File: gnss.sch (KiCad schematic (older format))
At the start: 12 parts, among them U2301 MAX-M8Q

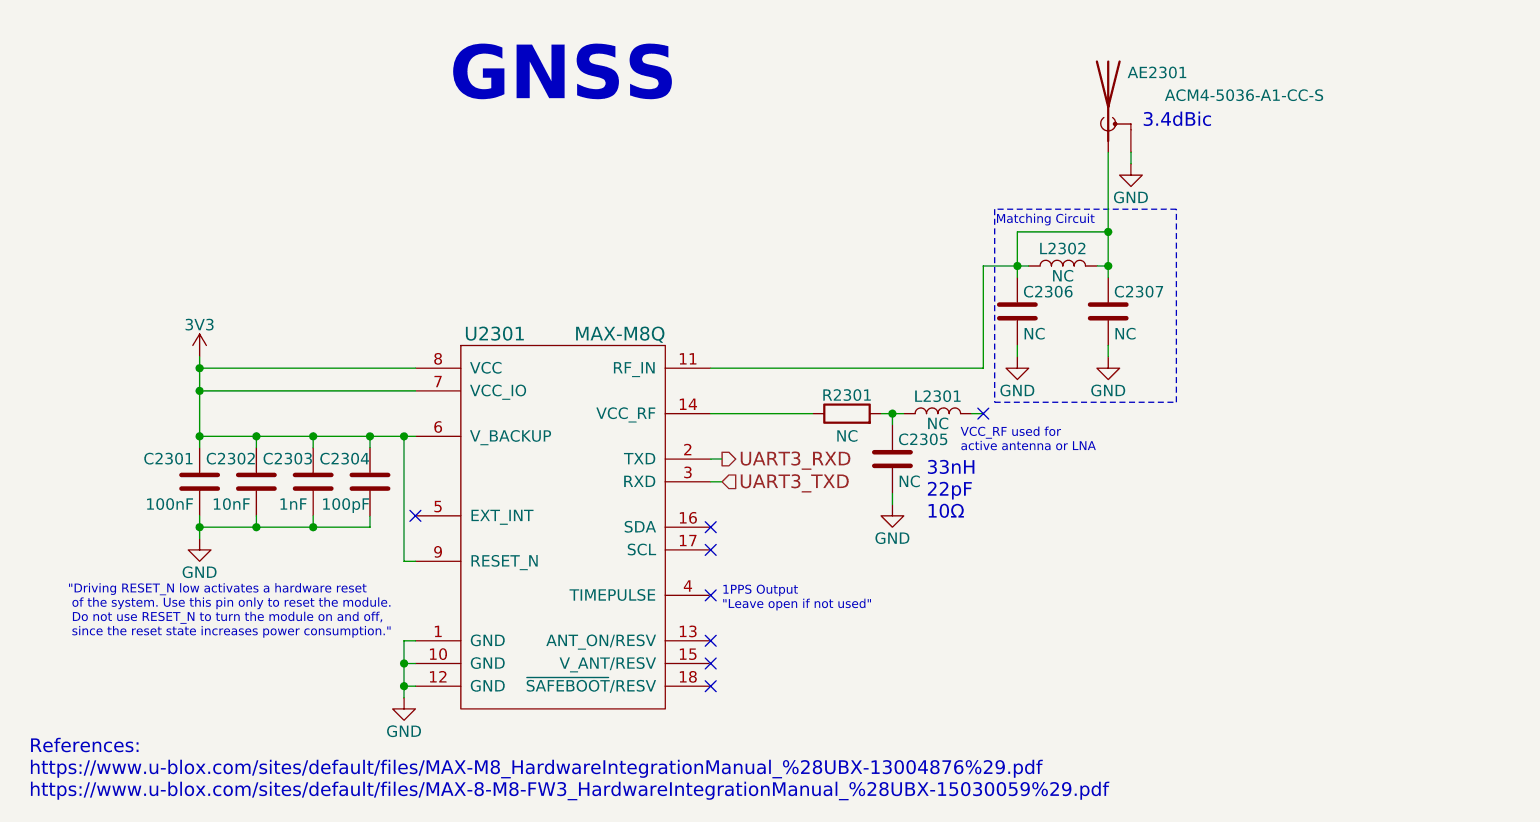
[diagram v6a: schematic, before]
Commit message: Add AC coupling caps to the HDMI_AUXP/N diff pair which were mistakenly left out, fix a couple typos/errors that were made when transitioning to the new top-leve sheet, make the M.2s' I2C RX TX hierarchical signals consistent and clearer
Hopefully all lingering errors have been caught, this will likely be the schematic commit that gets reviewed (fingers crossed).
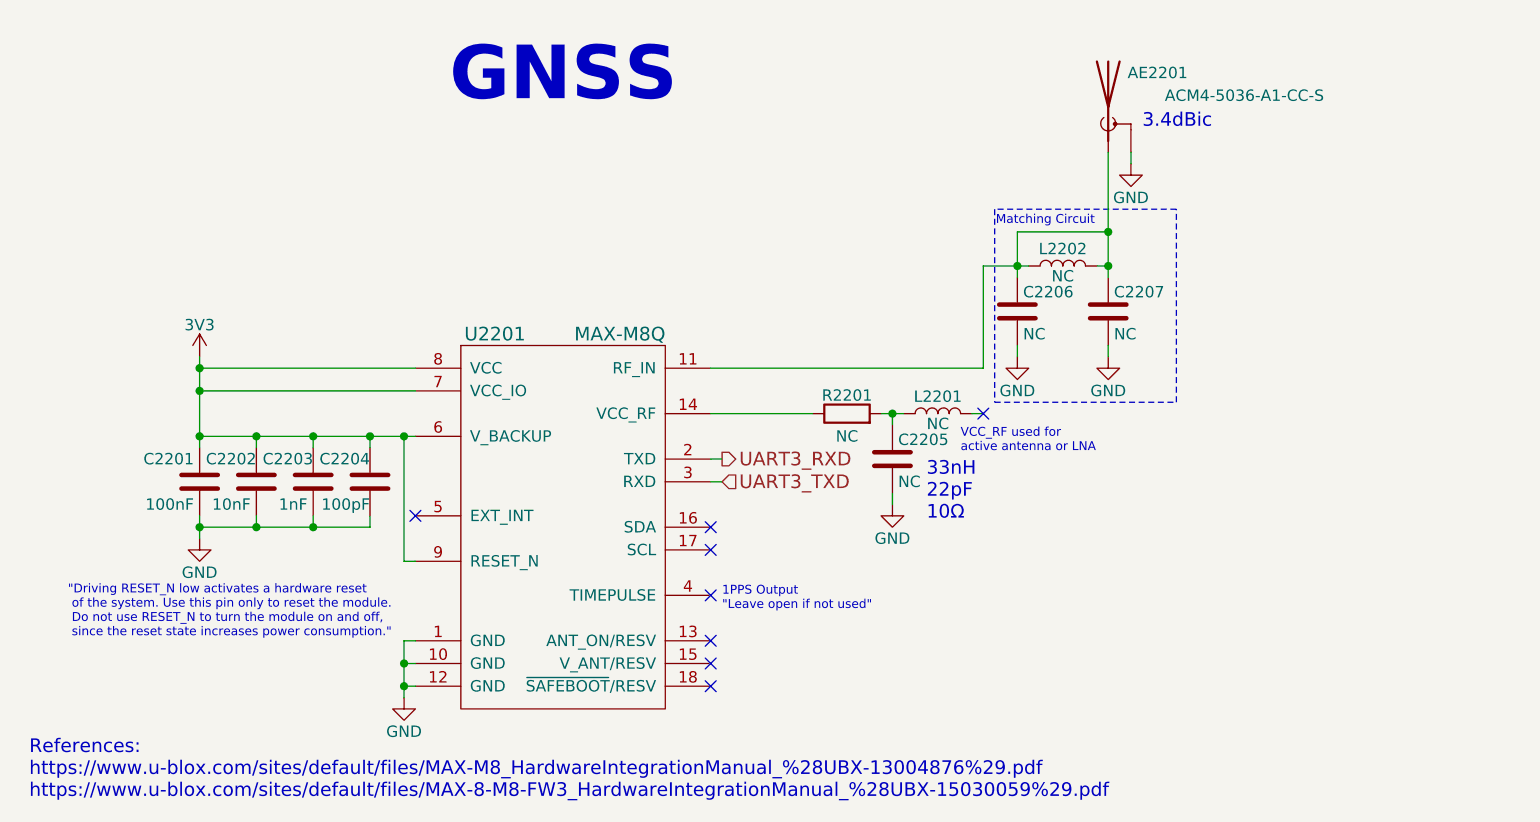
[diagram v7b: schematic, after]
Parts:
- renumbered AE2301 to AE2201, C2301 to C2201, C2302 to C2202, C2303 to C2203, C2304 to C2204, C2305 to C2205, C2306 to C2206, C2307 to C2207, L2301 to L2201, L2302 to L2202, R2301 to R2201, U2301 to U2201
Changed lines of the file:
@@
 $Descr A4 11693 8268
 encoding utf-8
-Sheet 23 24
+Sheet 22 24
 Title "GNSS"
 Date "2018-06-14"
@@
 $EndDescr
 $Comp
-L GND #PWR2303
+L GND #PWR0342
 U 1 1 5B0E0D78
 P 4800 4700
-F 0 "#PWR2303" H 4800 4450 50  0001 C CNN
+F 0 "#PWR0342" H 4800 4450 50  0001 C CNN
 F 1 "GND" H 4800 4550 50  0000 C CNN
 F 2 "" H 4800 4700 50  0001 C CNN
@@
 3.4dBic
 $Comp
-L 3V3 #PWR2301
+L 3V3 #PWR0343
 U 1 1 5B0E6D0E
 P 3900 3200
-F 0 "#PWR2301" H 3900 3050 50  0001 C CNN
+F 0 "#PWR0343" H 3900 3050 50  0001 C CNN
 F 1 "3V3" H 3900 3340 50  0000 C CNN
 F 2 "" H 3900 3200 50  0001 C CNN
@@
 NoConn ~ 6150 4450
 $Comp
-L C C2301
+L C C2201
 U 1 1 5B0ED9E5
 P 3900 3750
-F 0 "C2301" H 3925 3850 50  0000 L CNN
+F 0 "C2201" H 3925 3850 50  0000 L CNN
 F 1 "100nF" H 3925 3650 50  0000 L CNN
 F 2 "Capacitors_SMD:C_0603" H 3938 3600 50  0001 C CNN
@@
 $EndComp
 $Comp
-L GND #PWR2302
+L GND #PWR0344
 U 1 1 5B0EDAF7
 P 3900 4000
-F 0 "#PWR2302" H 3900 3750 50  0001 C CNN
+F 0 "#PWR0344" H 3900 3750 50  0001 C CNN
 F 1 "GND" H 3900 3850 50  0000 C CNN
 F 2 "" H 3900 4000 50  0001 C CNN
@@
 Connection ~ 4800 3550
 $Comp
-L C C2302
+L C C2202
 U 1 1 5B1028D6
 P 4150 3750
-F 0 "C2302" H 4150 3850 50  0000 L CNN
+F 0 "C2202" H 4150 3850 50  0000 L CNN
 F 1 "10nF" H 4175 3650 50  0000 L CNN
 F 2 "Capacitors_SMD:C_0603" H 4188 3600 50  0001 C CNN
@@
 $EndComp
 $Comp
-L C C2303
+L C C2203
 U 1 1 5B102929
 P 4400 3750
-F 0 "C2303" H 4400 3850 50  0000 L CNN
+F 0 "C2203" H 4400 3850 50  0000 L CNN
 F 1 "1nF" H 4425 3650 50  0000 L CNN
 F 2 "Capacitors_SMD:C_0603" H 4438 3600 50  0001 C CNN
@@
 $EndComp
 $Comp
-L C C2304
+L C C2204
 U 1 1 5B1029AE
 P 4650 3750
-F 0 "C2304" H 4650 3850 50  0000 L CNN
+F 0 "C2204" H 4650 3850 50  0000 L CNN
 F 1 "100pF" H 4650 3650 50  0000 L CNN
 F 2 "Capacitors_SMD:C_0603" H 4688 3600 50  0001 C CNN
@@
 UART3_TXD
 $Comp
-L Antenna_Chip AE2301
+L Antenna_Chip AE2201
 U 1 1 5B123EED
 P 7900 2100
-F 0 "AE2301" H 8250 2250 50  0000 R CNN
+F 0 "AE2201" H 8250 2250 50  0000 R CNN
 F 1 "ACM4-5036-A1-CC-S" H 8850 2150 50  0000 R CNN
 F 2 "dvk-mx8m-bsb:ACM4-5036-A1-CC-S" H 7900 2200 50  0001 C CNN
@@
 $EndComp
 $Comp
-L GND #PWR2307
+L GND #PWR0345
 U 1 1 5B12431F
 P 8000 2350
-F 0 "#PWR2307" H 8000 2100 50  0001 C CNN
+F 0 "#PWR0345" H 8000 2100 50  0001 C CNN
 F 1 "GND" H 8000 2200 50  0000 C CNN
 F 2 "" H 8000 2350 50  0001 C CNN
@@
 	7350 3450 7300 3450
 $Comp
-L L L2301
+L L L2201
 U 1 1 5B103CD2
 P 7150 3450
-F 0 "L2301" V 7225 3450 50  0000 C CNN
+F 0 "L2201" V 7225 3450 50  0000 C CNN
 F 1 "NC" V 7105 3450 50  0000 C CNN
 F 2 "Inductors_SMD:L_0603" H 7150 3450 50  0001 C CNN
@@
 	6950 3850 6950 3800
 $Comp
-L GND #PWR2304
+L GND #PWR0346
 U 1 1 5B103EA0
 P 6950 3850
-F 0 "#PWR2304" H 6950 3600 50  0001 C CNN
+F 0 "#PWR0346" H 6950 3600 50  0001 C CNN
 F 1 "GND" H 6950 3700 50  0000 C CNN
 F 2 "" H 6950 3850 50  0001 C CNN
@@
 	6900 3450 7000 3450
 $Comp
-L C C2305
+L C C2205
 U 1 1 5B103D07
 P 6950 3650
-F 0 "C2305" H 6975 3735 50  0000 L CNN
+F 0 "C2205" H 6975 3735 50  0000 L CNN
 F 1 "NC" H 6975 3550 50  0000 L CNN
 F 2 "Capacitors_SMD:C_0603" H 6988 3500 50  0001 C CNN
@@
 $EndComp
 $Comp
-L R R2301
+L R R2201
 U 1 1 5B103CA5
 P 6750 3450
-F 0 "R2301" V 6830 3450 50  0000 C CNN
+F 0 "R2201" V 6830 3450 50  0000 C CNN
 F 1 "NC" V 6650 3450 50  0000 C CNN
 F 2 "Resistors_SMD:R_0603" V 6680 3450 50  0001 C CNN
@@
 33nH\n22pF\n10Ω
 $Comp
-L L L2302
+L L L2202
 U 1 1 5B2088FC
 P 7700 2800
-F 0 "L2302" V 7775 2800 50  0000 C CNN
+F 0 "L2202" V 7775 2800 50  0000 C CNN
 F 1 "NC" V 7655 2800 50  0000 C CNN
 F 2 "Inductors_SMD:L_0603" H 7700 2800 50  0001 C CNN
@@
 	7500 3200 7500 3150
 $Comp
-L GND #PWR2305
+L GND #PWR0347
 U 1 1 5B208BC0
 P 7500 3200
-F 0 "#PWR2305" H 7500 2950 50  0001 C CNN
+F 0 "#PWR0347" H 7500 2950 50  0001 C CNN
 F 1 "GND" H 7500 3050 50  0000 C CNN
 F 2 "" H 7500 3200 50  0001 C CNN
@@
 $EndComp
 $Comp
-L C C2306
+L C C2206
 U 1 1 5B208BC6
 P 7500 3000
-F 0 "C2306" H 7525 3085 50  0000 L CNN
+F 0 "C2206" H 7525 3085 50  0000 L CNN
 F 1 "NC" H 7525 2900 50  0000 L CNN
 F 2 "Capacitors_SMD:C_0603" H 7538 2850 50  0001 C CNN
@@
 	7900 3200 7900 3150
 $Comp
-L GND #PWR2306
+L GND #PWR0348
 U 1 1 5B208DA1
 P 7900 3200
-F 0 "#PWR2306" H 7900 2950 50  0001 C CNN
+F 0 "#PWR0348" H 7900 2950 50  0001 C CNN
 F 1 "GND" H 7900 3050 50  0000 C CNN
 F 2 "" H 7900 3200 50  0001 C CNN
@@
 $EndComp
 $Comp
-L C C2307
+L C C2207
 U 1 1 5B208DA7
 P 7900 3000
-F 0 "C2307" H 7925 3085 50  0000 L CNN
+F 0 "C2207" H 7925 3085 50  0000 L CNN
 F 1 "NC" H 7925 2900 50  0000 L CNN
 F 2 "Capacitors_SMD:C_0603" H 7938 2850 50  0001 C CNN
@@
 GNSS
 $Comp
-L MAX-M8 U2301
+L MAX-M8 U2201
 U 1 1 5B0DFDBF
 P 5500 3950
-F 0 "U2301" H 5200 4800 60  0000 C CNN
+F 0 "U2201" H 5200 4800 60  0000 C CNN
 F 1 "MAX-M8Q" H 5750 4800 60  0000 C CNN
 F 2 "dvk-mx8m-bsb:MAX-M8" H 6350 4300 60  0001 C CNN

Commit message: Move the WLAN+BT M.2 sheet back to page 18 rather than the last page (24)
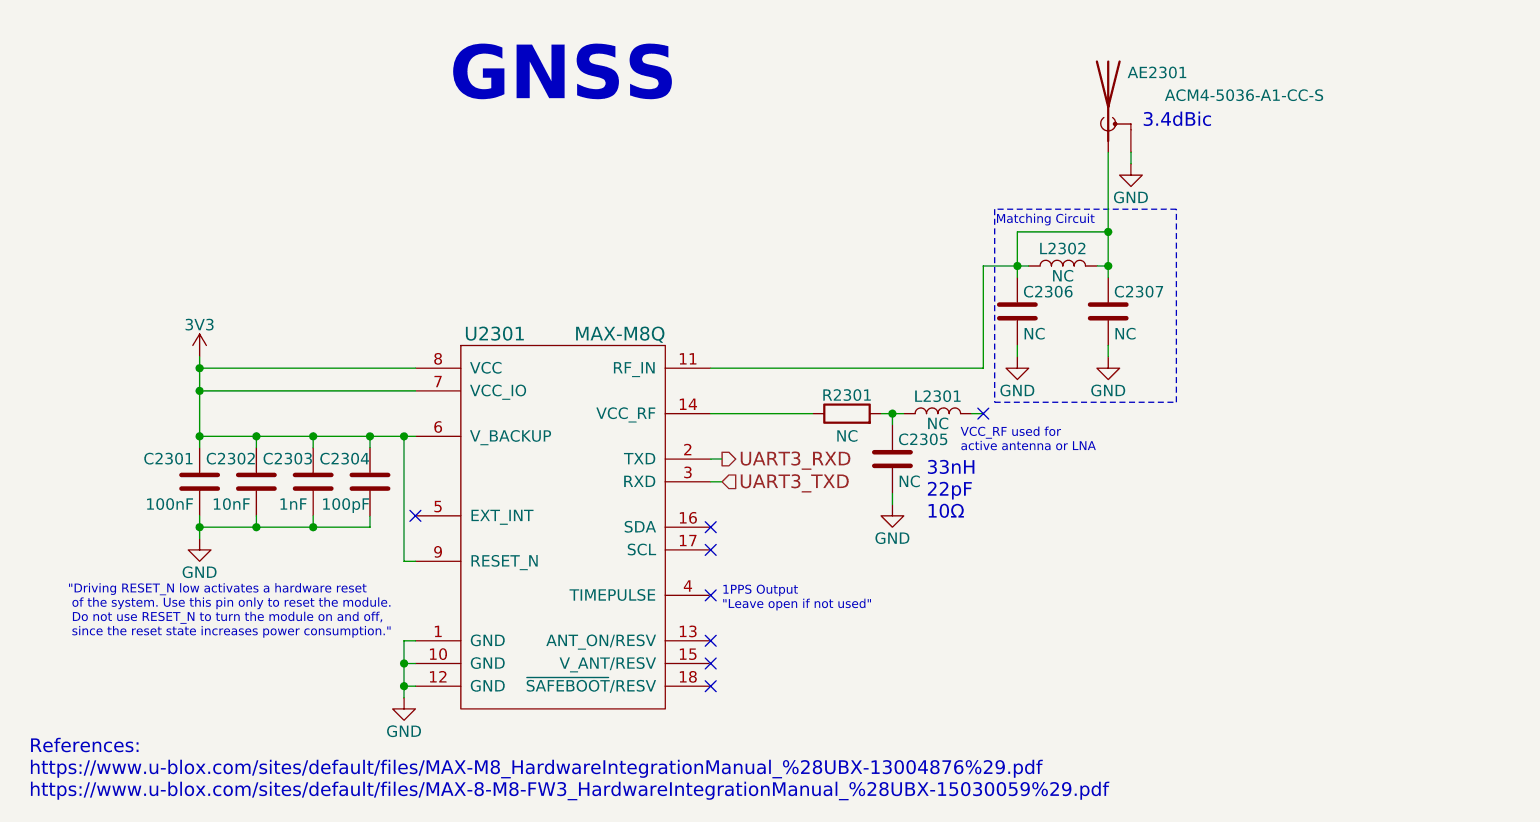
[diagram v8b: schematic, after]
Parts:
- renumbered AE2201 to AE2301, C2201 to C2301, C2202 to C2302, C2203 to C2303, C2204 to C2304, C2205 to C2305, C2206 to C2306, C2207 to C2307, L2201 to L2301, L2202 to L2302, R2201 to R2301, U2201 to U2301
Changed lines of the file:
@@
 $Descr A4 11693 8268
 encoding utf-8
-Sheet 22 24
+Sheet 23 24
 Title "GNSS"
-Date "2018-06-14"
+Date "2018-06-15"
 Rev "v0.1.0"
 Comp "Copyright 2018 GNU GPLv3"
@@
 $EndDescr
 $Comp
-L GND #PWR0342
+L GND #PWR0368
 U 1 1 5B0E0D78
 P 4800 4700
-F 0 "#PWR0342" H 4800 4450 50  0001 C CNN
+F 0 "#PWR0368" H 4800 4450 50  0001 C CNN
 F 1 "GND" H 4800 4550 50  0000 C CNN
 F 2 "" H 4800 4700 50  0001 C CNN
@@
 3.4dBic
 $Comp
-L 3V3 #PWR0343
+L 3V3 #PWR0369
 U 1 1 5B0E6D0E
 P 3900 3200
-F 0 "#PWR0343" H 3900 3050 50  0001 C CNN
+F 0 "#PWR0369" H 3900 3050 50  0001 C CNN
 F 1 "3V3" H 3900 3340 50  0000 C CNN
 F 2 "" H 3900 3200 50  0001 C CNN
@@
 NoConn ~ 6150 4450
 $Comp
-L C C2201
+L C C2301
 U 1 1 5B0ED9E5
 P 3900 3750
-F 0 "C2201" H 3925 3850 50  0000 L CNN
+F 0 "C2301" H 3925 3850 50  0000 L CNN
 F 1 "100nF" H 3925 3650 50  0000 L CNN
 F 2 "Capacitors_SMD:C_0603" H 3938 3600 50  0001 C CNN
@@
 $EndComp
 $Comp
-L GND #PWR0344
+L GND #PWR0370
 U 1 1 5B0EDAF7
 P 3900 4000
-F 0 "#PWR0344" H 3900 3750 50  0001 C CNN
+F 0 "#PWR0370" H 3900 3750 50  0001 C CNN
 F 1 "GND" H 3900 3850 50  0000 C CNN
 F 2 "" H 3900 4000 50  0001 C CNN
@@
 Connection ~ 4800 3550
 $Comp
-L C C2202
+L C C2302
 U 1 1 5B1028D6
 P 4150 3750
-F 0 "C2202" H 4150 3850 50  0000 L CNN
+F 0 "C2302" H 4150 3850 50  0000 L CNN
 F 1 "10nF" H 4175 3650 50  0000 L CNN
 F 2 "Capacitors_SMD:C_0603" H 4188 3600 50  0001 C CNN
@@
 $EndComp
 $Comp
-L C C2203
+L C C2303
 U 1 1 5B102929
 P 4400 3750
-F 0 "C2203" H 4400 3850 50  0000 L CNN
+F 0 "C2303" H 4400 3850 50  0000 L CNN
 F 1 "1nF" H 4425 3650 50  0000 L CNN
 F 2 "Capacitors_SMD:C_0603" H 4438 3600 50  0001 C CNN
@@
 $EndComp
 $Comp
-L C C2204
+L C C2304
 U 1 1 5B1029AE
 P 4650 3750
-F 0 "C2204" H 4650 3850 50  0000 L CNN
+F 0 "C2304" H 4650 3850 50  0000 L CNN
 F 1 "100pF" H 4650 3650 50  0000 L CNN
 F 2 "Capacitors_SMD:C_0603" H 4688 3600 50  0001 C CNN
@@
 UART3_TXD
 $Comp
-L Antenna_Chip AE2201
+L Antenna_Chip AE2301
 U 1 1 5B123EED
 P 7900 2100
-F 0 "AE2201" H 8250 2250 50  0000 R CNN
+F 0 "AE2301" H 8250 2250 50  0000 R CNN
 F 1 "ACM4-5036-A1-CC-S" H 8850 2150 50  0000 R CNN
 F 2 "dvk-mx8m-bsb:ACM4-5036-A1-CC-S" H 7900 2200 50  0001 C CNN
@@
 $EndComp
 $Comp
-L GND #PWR0345
+L GND #PWR0371
 U 1 1 5B12431F
 P 8000 2350
-F 0 "#PWR0345" H 8000 2100 50  0001 C CNN
+F 0 "#PWR0371" H 8000 2100 50  0001 C CNN
 F 1 "GND" H 8000 2200 50  0000 C CNN
 F 2 "" H 8000 2350 50  0001 C CNN
@@
 	7350 3450 7300 3450
 $Comp
-L L L2201
+L L L2301
 U 1 1 5B103CD2
 P 7150 3450
-F 0 "L2201" V 7225 3450 50  0000 C CNN
+F 0 "L2301" V 7225 3450 50  0000 C CNN
 F 1 "NC" V 7105 3450 50  0000 C CNN
 F 2 "Inductors_SMD:L_0603" H 7150 3450 50  0001 C CNN
@@
 	6950 3850 6950 3800
 $Comp
-L GND #PWR0346
+L GND #PWR0372
 U 1 1 5B103EA0
 P 6950 3850
-F 0 "#PWR0346" H 6950 3600 50  0001 C CNN
+F 0 "#PWR0372" H 6950 3600 50  0001 C CNN
 F 1 "GND" H 6950 3700 50  0000 C CNN
 F 2 "" H 6950 3850 50  0001 C CNN
@@
 	6900 3450 7000 3450
 $Comp
-L C C2205
+L C C2305
 U 1 1 5B103D07
 P 6950 3650
-F 0 "C2205" H 6975 3735 50  0000 L CNN
+F 0 "C2305" H 6975 3735 50  0000 L CNN
 F 1 "NC" H 6975 3550 50  0000 L CNN
 F 2 "Capacitors_SMD:C_0603" H 6988 3500 50  0001 C CNN
@@
 $EndComp
 $Comp
-L R R2201
+L R R2301
 U 1 1 5B103CA5
 P 6750 3450
-F 0 "R2201" V 6830 3450 50  0000 C CNN
+F 0 "R2301" V 6830 3450 50  0000 C CNN
 F 1 "NC" V 6650 3450 50  0000 C CNN
 F 2 "Resistors_SMD:R_0603" V 6680 3450 50  0001 C CNN
@@
 33nH\n22pF\n10Ω
 $Comp
-L L L2202
+L L L2302
 U 1 1 5B2088FC
 P 7700 2800
-F 0 "L2202" V 7775 2800 50  0000 C CNN
+F 0 "L2302" V 7775 2800 50  0000 C CNN
 F 1 "NC" V 7655 2800 50  0000 C CNN
 F 2 "Inductors_SMD:L_0603" H 7700 2800 50  0001 C CNN
@@
 	7500 3200 7500 3150
 $Comp
-L GND #PWR0347
+L GND #PWR0373
 U 1 1 5B208BC0
 P 7500 3200
-F 0 "#PWR0347" H 7500 2950 50  0001 C CNN
+F 0 "#PWR0373" H 7500 2950 50  0001 C CNN
 F 1 "GND" H 7500 3050 50  0000 C CNN
 F 2 "" H 7500 3200 50  0001 C CNN
@@
 $EndComp
 $Comp
-L C C2206
+L C C2306
 U 1 1 5B208BC6
 P 7500 3000
-F 0 "C2206" H 7525 3085 50  0000 L CNN
+F 0 "C2306" H 7525 3085 50  0000 L CNN
 F 1 "NC" H 7525 2900 50  0000 L CNN
 F 2 "Capacitors_SMD:C_0603" H 7538 2850 50  0001 C CNN
@@
 	7900 3200 7900 3150
 $Comp
-L GND #PWR0348
+L GND #PWR0374
 U 1 1 5B208DA1
 P 7900 3200
-F 0 "#PWR0348" H 7900 2950 50  0001 C CNN
+F 0 "#PWR0374" H 7900 2950 50  0001 C CNN
 F 1 "GND" H 7900 3050 50  0000 C CNN
 F 2 "" H 7900 3200 50  0001 C CNN
@@
 $EndComp
 $Comp
-L C C2207
+L C C2307
 U 1 1 5B208DA7
 P 7900 3000
-F 0 "C2207" H 7925 3085 50  0000 L CNN
+F 0 "C2307" H 7925 3085 50  0000 L CNN
 F 1 "NC" H 7925 2900 50  0000 L CNN
 F 2 "Capacitors_SMD:C_0603" H 7938 2850 50  0001 C CNN
@@
 GNSS
 $Comp
-L MAX-M8 U2201
+L MAX-M8 U2301
 U 1 1 5B0DFDBF
 P 5500 3950
-F 0 "U2201" H 5200 4800 60  0000 C CNN
+F 0 "U2301" H 5200 4800 60  0000 C CNN
 F 1 "MAX-M8Q" H 5750 4800 60  0000 C CNN
 F 2 "dvk-mx8m-bsb:MAX-M8" H 6350 4300 60  0001 C CNN
